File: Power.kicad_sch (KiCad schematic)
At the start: 33 parts, among them J1 Jack-DC, J2 USB_B_Micro, U1 LM2596S-5, U3 LM1117-3.3, U4 LM1117-1.8, U5 TPS2552DBVR

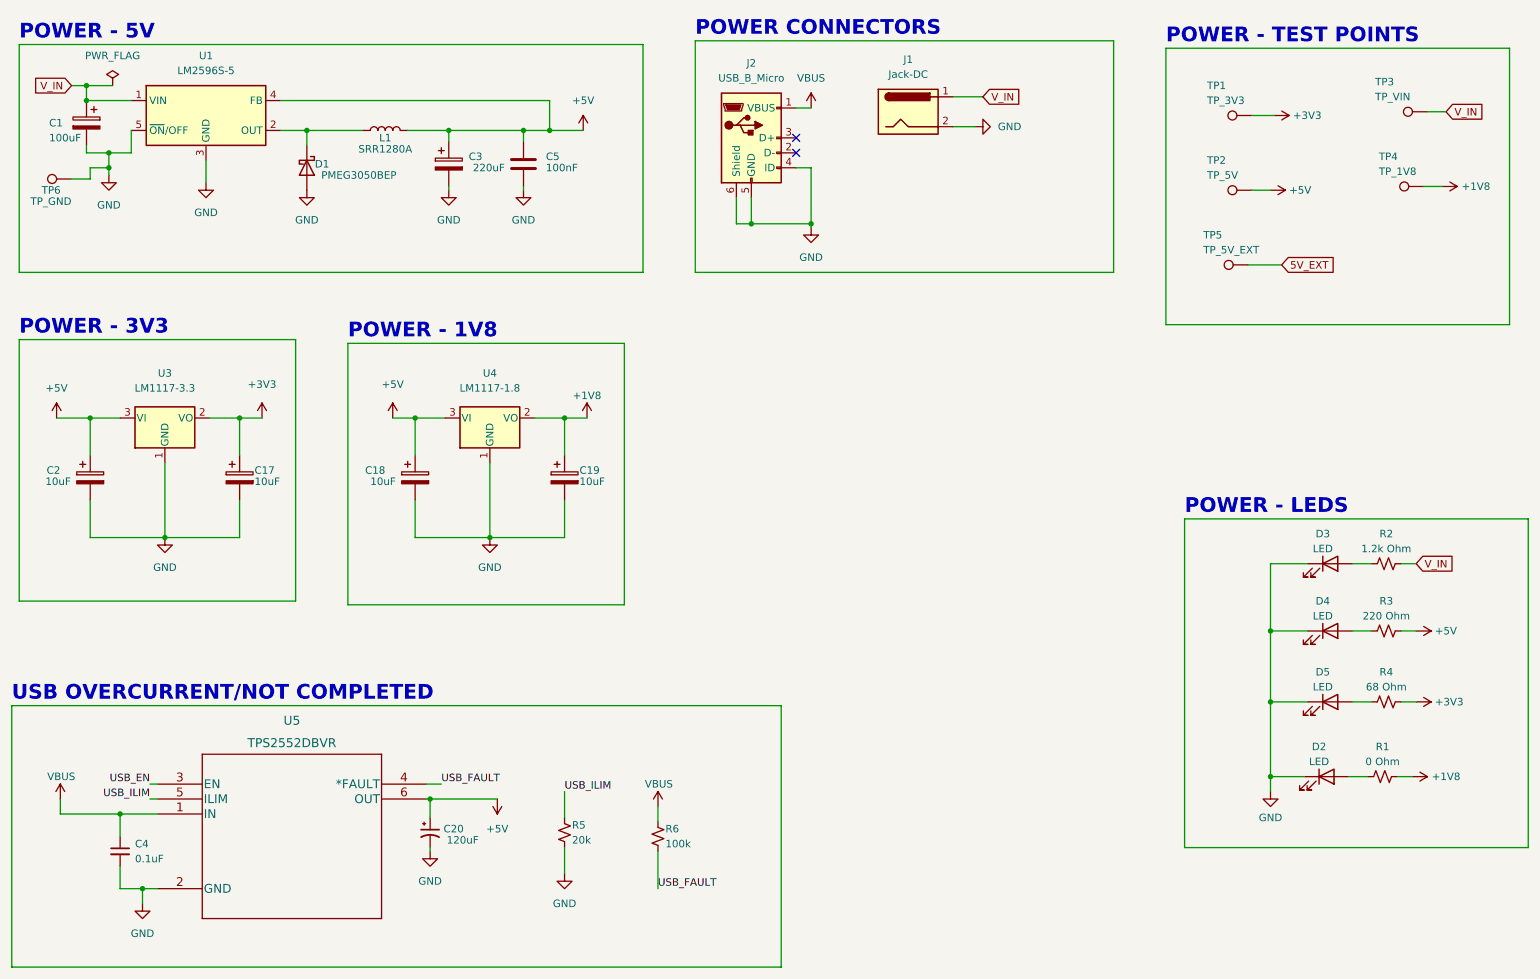
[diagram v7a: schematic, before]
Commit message: ISP Boot eklenecek
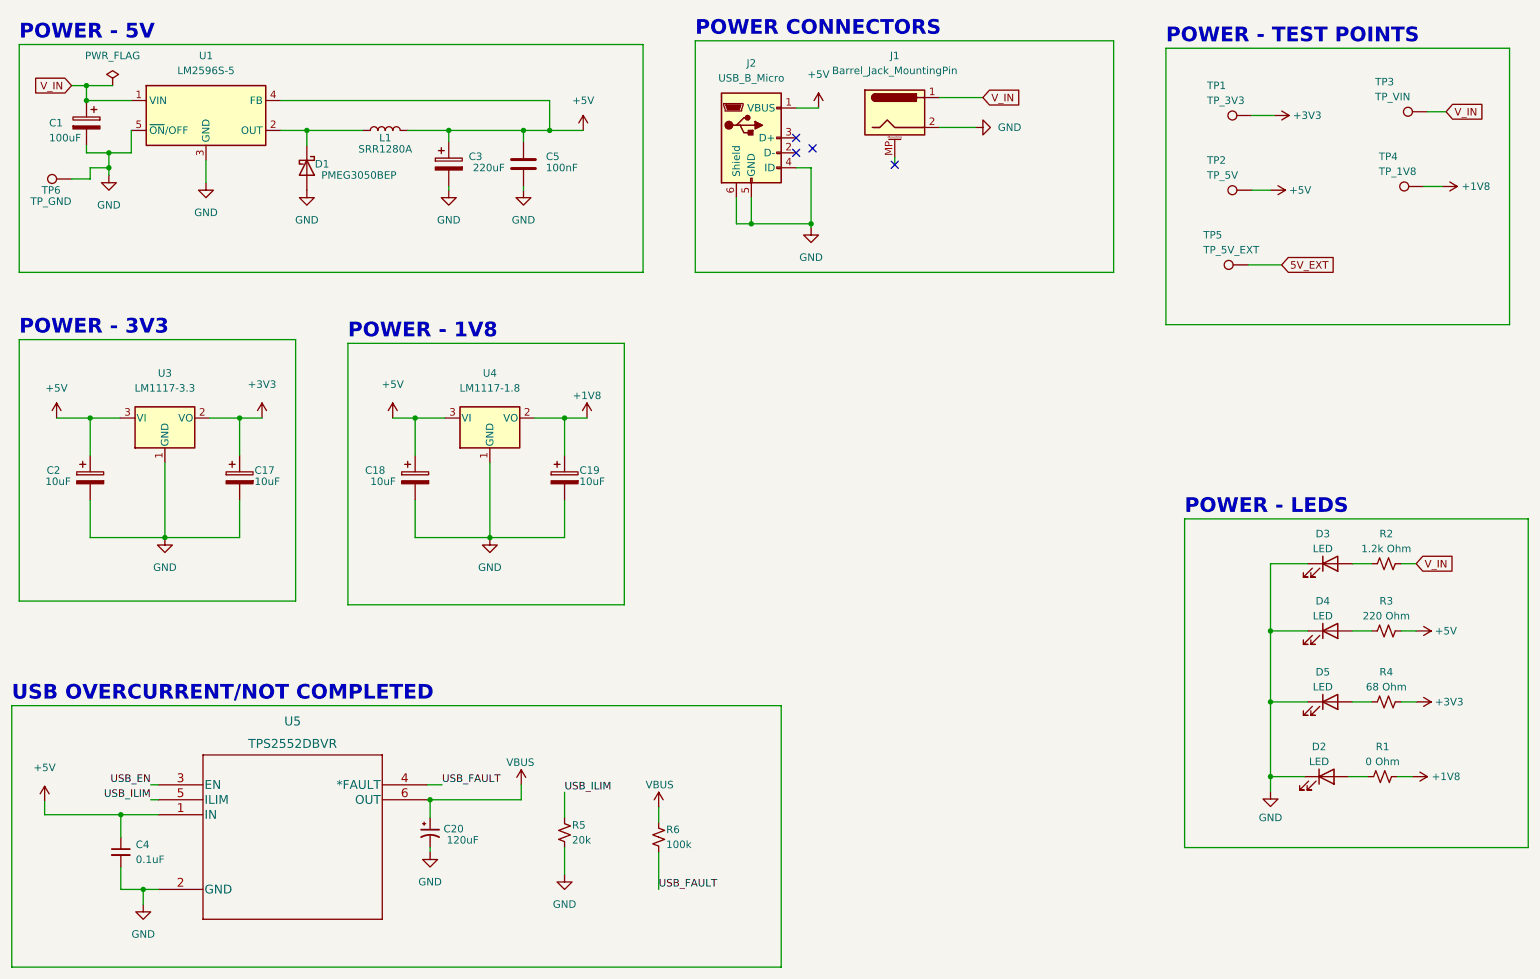
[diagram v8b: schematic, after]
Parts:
- removed J1: Jack-DC, erkan-hw-lib:DC-JACK-5.5x2.1, symbol Connector:Jack-DC
- added J1: Barrel_Jack_MountingPin, erkan-hw-lib:DC-JACK-5.5x2.1, symbol Connector:Barrel_Jack_MountingPin
- C20: footprint (none) -> Capacitor_Tantalum_SMD:CP_EIA-6032-28_Kemet-C
- C5: footprint Capacitor_SMD:C_0805_2012Metric -> Capacitor_SMD:C_0603_1608Metric
- D1: footprint erkan-hw-lib:D_SOD-128 -> Diode_SMD:D_SOD-128
- U5: footprint erkan-hw-lib:HPA00714DBVR -> erkan-hw-lib:TPS2552DBVR
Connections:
- net +5V: now also C4.1, J2.1 (VBUS), U5.1 (IN); no longer C20.1, U5.6 (OUT)
- net GND: now also J1.2
- net VBUS: now also C20.1, U5.6 (OUT); no longer C4.1, J2.1 (VBUS), U5.1 (IN)
- net V_IN: now also J1.1
- no-connect marks 2 -> 4
